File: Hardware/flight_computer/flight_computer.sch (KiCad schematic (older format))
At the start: 15 parts

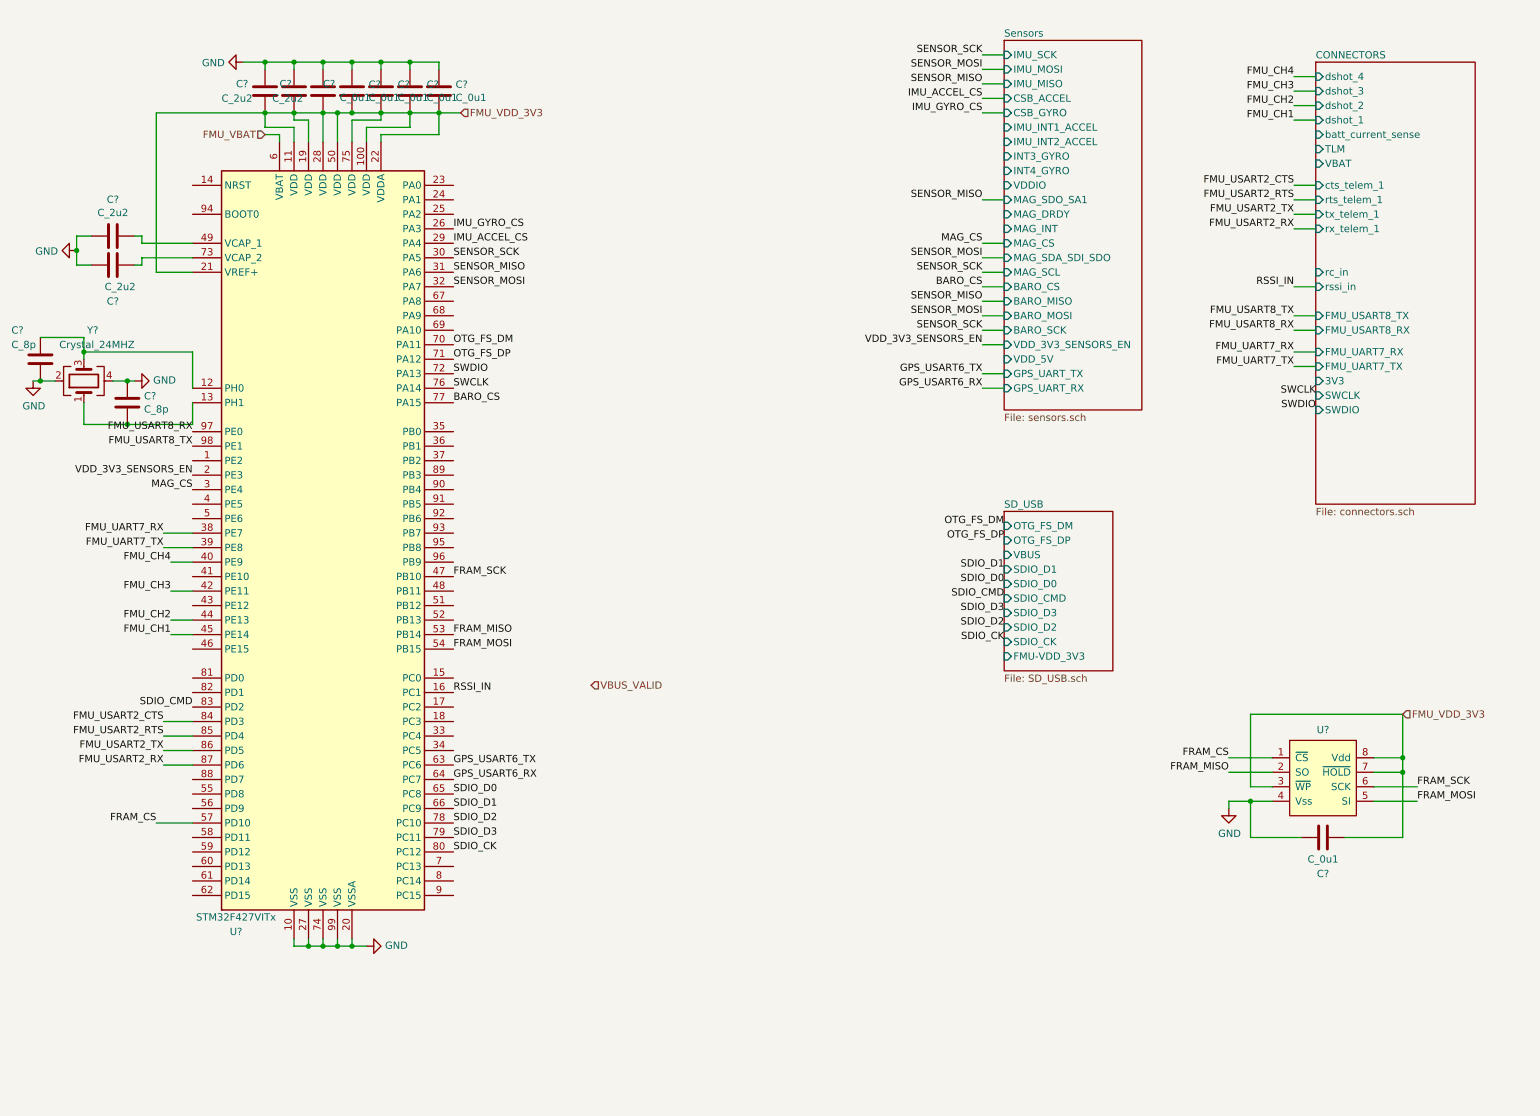
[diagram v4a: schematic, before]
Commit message: Updates drdy pins and rc connections
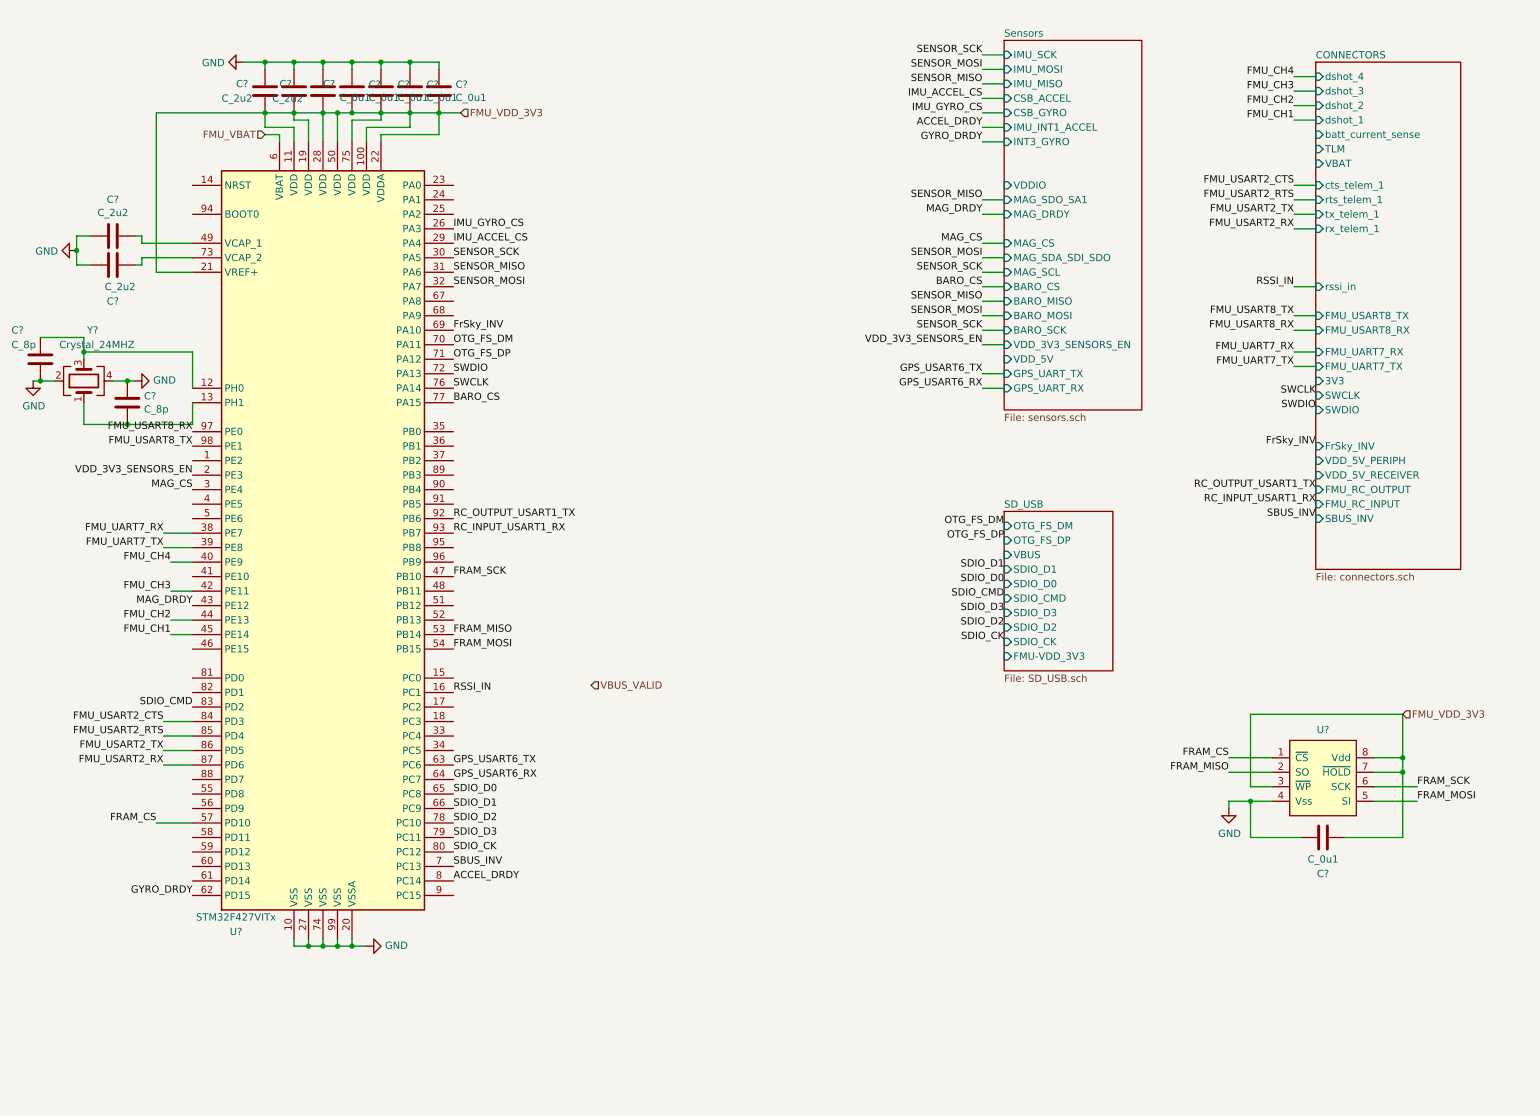
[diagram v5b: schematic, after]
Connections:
- net MAG_DRDY: now reaches U?.43 (PE12)
- net GYRO_DRDY: now reaches U?.62 (PD15)
- net FrSky_INV: now reaches U?.69 (PA10)
- net SBUS_INV: now reaches U?.7 (PC13)
- net ACCEL_DRDY: now reaches U?.8 (PC14)
- net RC_OUTPUT_USART1_TX: now reaches U?.92 (PB6)
- net RC_INPUT_USART1_RX: now reaches U?.93 (PB7)
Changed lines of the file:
@@
 F6 "CSB_GYRO" I L 7550 1150 50
 F7 "IMU_INT1_ACCEL" I L 7550 1250 50
-F8 "IMU_INT2_ACCEL" I L 7550 1350 50
-F9 "INT3_GYRO" I L 7550 1450 50
-F10 "INT4_GYRO" I L 7550 1550 50
+F9 "INT3_GYRO" I L 7550 1350 50
 F11 "VDDIO" I L 7550 1650 50
 F12 "MAG_SDO_SA1" I L 7550 1750 50
 F13 "MAG_DRDY" I L 7550 1850 50
-F14 "MAG_INT" I L 7550 1950 50
 F15 "MAG_CS" I L 7550 2050 50
 F16 "MAG_SDA_SDI_SDO" I L 7550 2150 50
@@
 VDD_3V3_SENSORS_EN
 $Sheet
-S 9700 800  1100 3050
+S 9700 800  1000 3500
 U 5F7684E9
 F0 "CONNECTORS" 50
@@
 F11 "cts_telem_1" I L 9700 1650 50
 F12 "rts_telem_1" I L 9700 1750 50
-F13 "rc_in" I L 9700 2250 50
 F14 "rssi_in" I L 9700 2350 50
 F15 "FMU_UART7_RX" I L 9700 2800 50
@@
 F20 "FMU_USART8_TX" I L 9700 2550 50
 F21 "FMU_USART8_RX" I L 9700 2650 50
+F22 "FrSky_INV" I L 9700 3450 50
+F23 "VDD_5V_PERIPH" I L 9700 3550 50
+F24 "VDD_5V_RECEIVER" I L 9700 3650 50
+F25 "FMU_RC_OUTPUT" I L 9700 3750 50
+F26 "FMU_RC_INPUT" I L 9700 3850 50
+F27 "SBUS_INV" I L 9700 3950 50
 $EndSheet
 Text Label 7400 1050 2    50   ~ 0
@@
 Text Label 9700 3100 2    50   ~ 0
 SWCLK
+Text Label 3750 6450 0    50   ~ 0
+ACCEL_DRDY
+Text Label 1950 6550 2    50   ~ 0
+GYRO_DRDY
+Text Label 1950 4550 2    50   ~ 0
+MAG_DRDY
+Text Label 7400 1250 2    50   ~ 0
+ACCEL_DRDY
+Text Label 7400 1350 2    50   ~ 0
+GYRO_DRDY
+Text Label 7400 1850 2    50   ~ 0
+MAG_DRDY
+Wire Wire Line
+	7550 1850 7400 1850
+Wire Wire Line
+	7550 1250 7400 1250
+Wire Wire Line
+	7550 1350 7400 1350
+Text Label 3750 6350 0    50   ~ 0
+SBUS_INV
+Text Label 9700 3950 2    50   ~ 0
+SBUS_INV
+Text Label 3750 2650 0    50   ~ 0
+FrSky_INV
+Text Label 9700 3450 2    50   ~ 0
+FrSky_INV
+Text Label 3750 4050 0    50   ~ 0
+RC_INPUT_USART1_RX
+Text Label 3750 3950 0    50   ~ 0
+RC_OUTPUT_USART1_TX
+Text Label 9700 3850 2    50   ~ 0
+RC_INPUT_USART1_RX
+Text Label 9700 3750 2    50   ~ 0
+RC_OUTPUT_USART1_TX
 $EndSCHEMATC

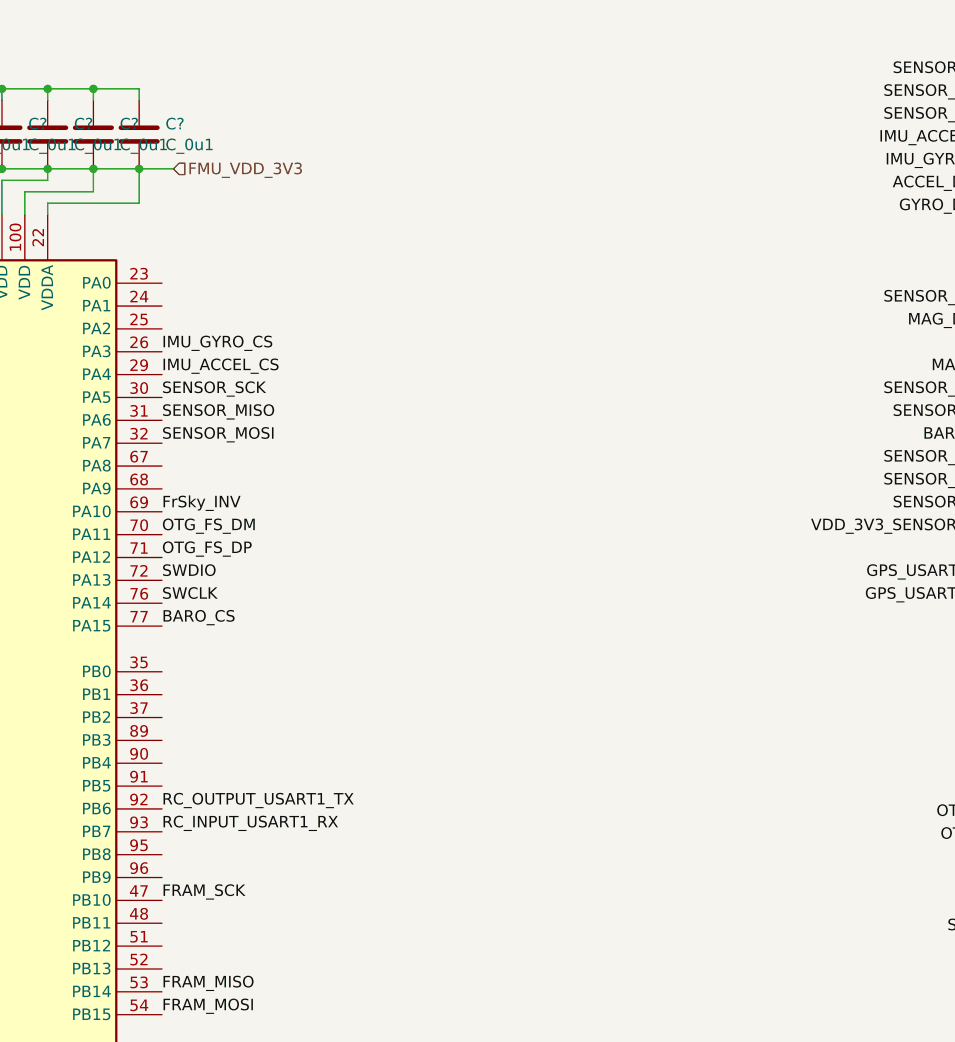
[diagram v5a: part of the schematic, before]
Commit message: Adds raspi i2c
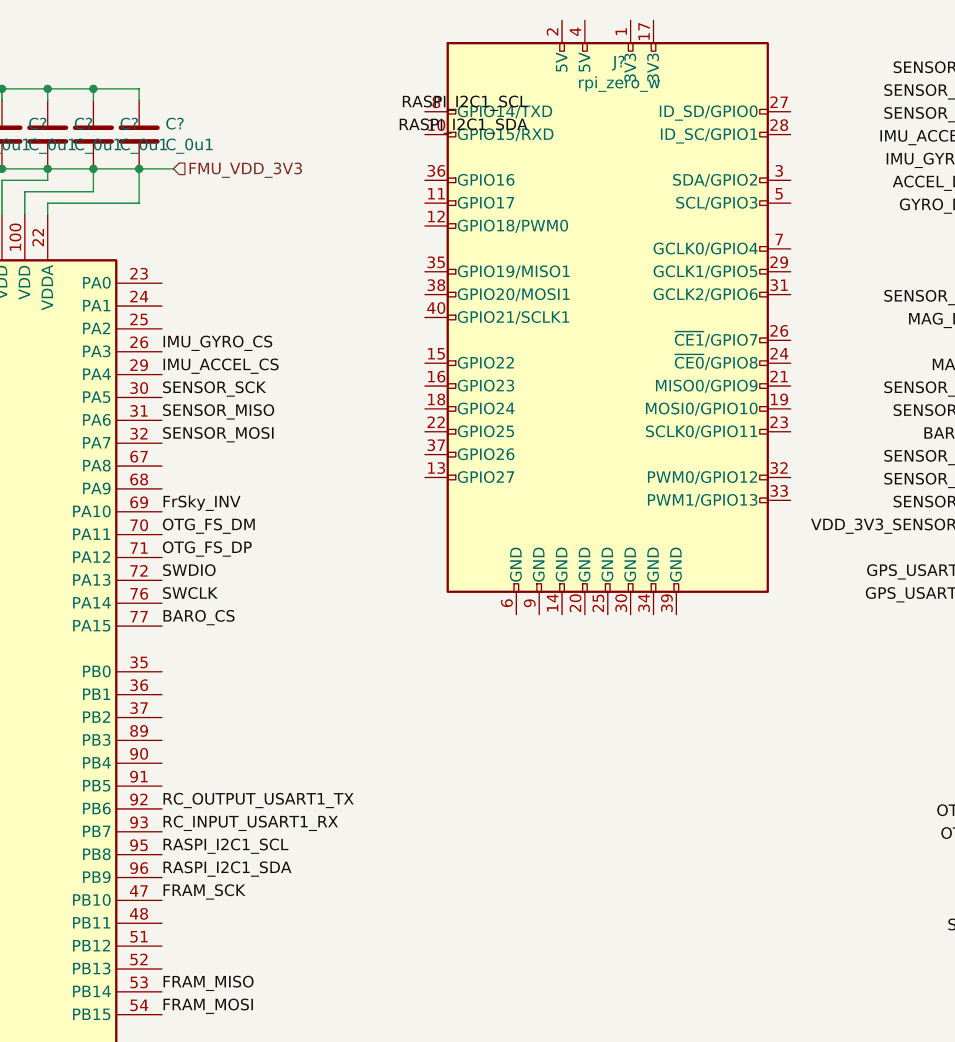
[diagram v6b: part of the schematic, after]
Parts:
- added J?: rpi_zero_w, drone_footprints:rpi_zero_w, symbol openDrone_parts:rpi_zero_w
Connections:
- net RASPI_I2C1_SCL: now reaches U?.95 (PB8)
- net RASPI_I2C1_SDA: now reaches U?.96 (PB9)
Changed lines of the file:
@@
 Text Label 9700 3750 2    50   ~ 0
 RC_OUTPUT_USART1_TX
+Text Label 3750 4150 0    50   ~ 0
+RASPI_I2C1_SCL
+Text Label 3750 4250 0    50   ~ 0
+RASPI_I2C1_SDA
+Text Label 5350 900  2    50   ~ 0
+RASPI_I2C1_SCL
+Text Label 5350 1000 2    50   ~ 0
+RASPI_I2C1_SDA
+$Comp
+L openDrone_parts:rpi_zero_w J?
+U 1 1 5F812ED0
+P 5700 1800
+F 0 "J?" H 5750 2917 50  0000 C CNN
+F 1 "rpi_zero_w" H 5750 2826 50  0000 C CNN
+F 2 "drone_footprints:rpi_zero_w" H 5700 1800 50  0001 C CNN
+F 3 "~" H 5700 1800 50  0001 C CNN
+	1    5700 1800
+	1    0    0    -1
+$EndComp
 $EndSCHEMATC

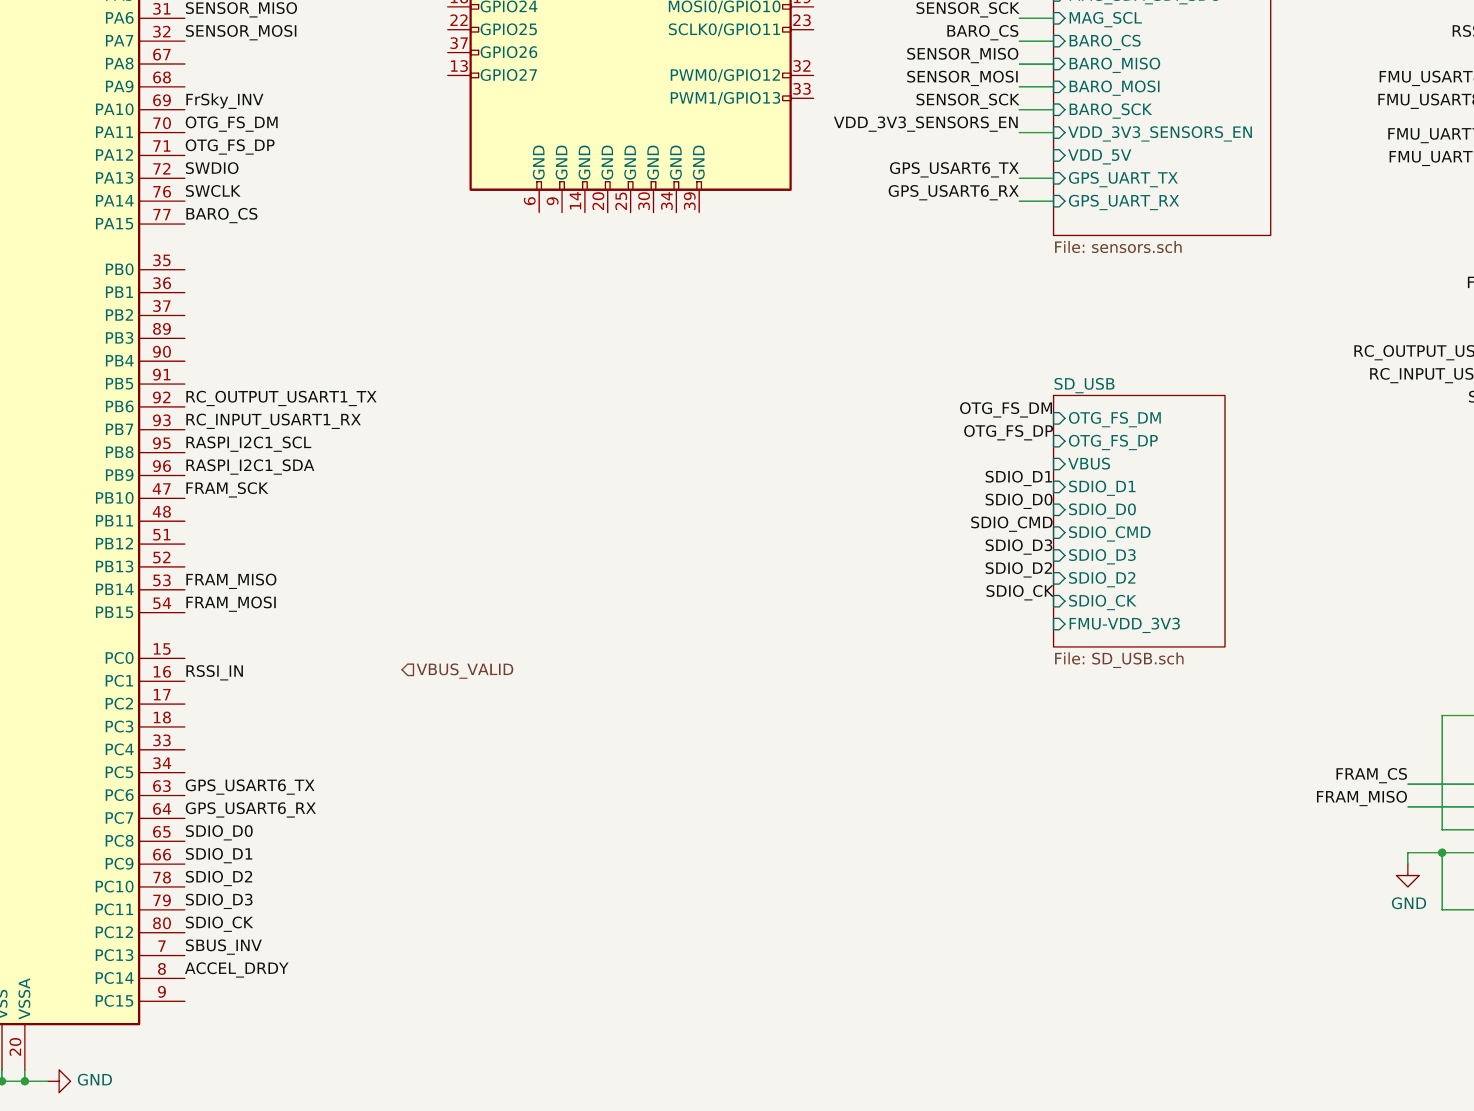
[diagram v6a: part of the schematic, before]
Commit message: Adds buck converters
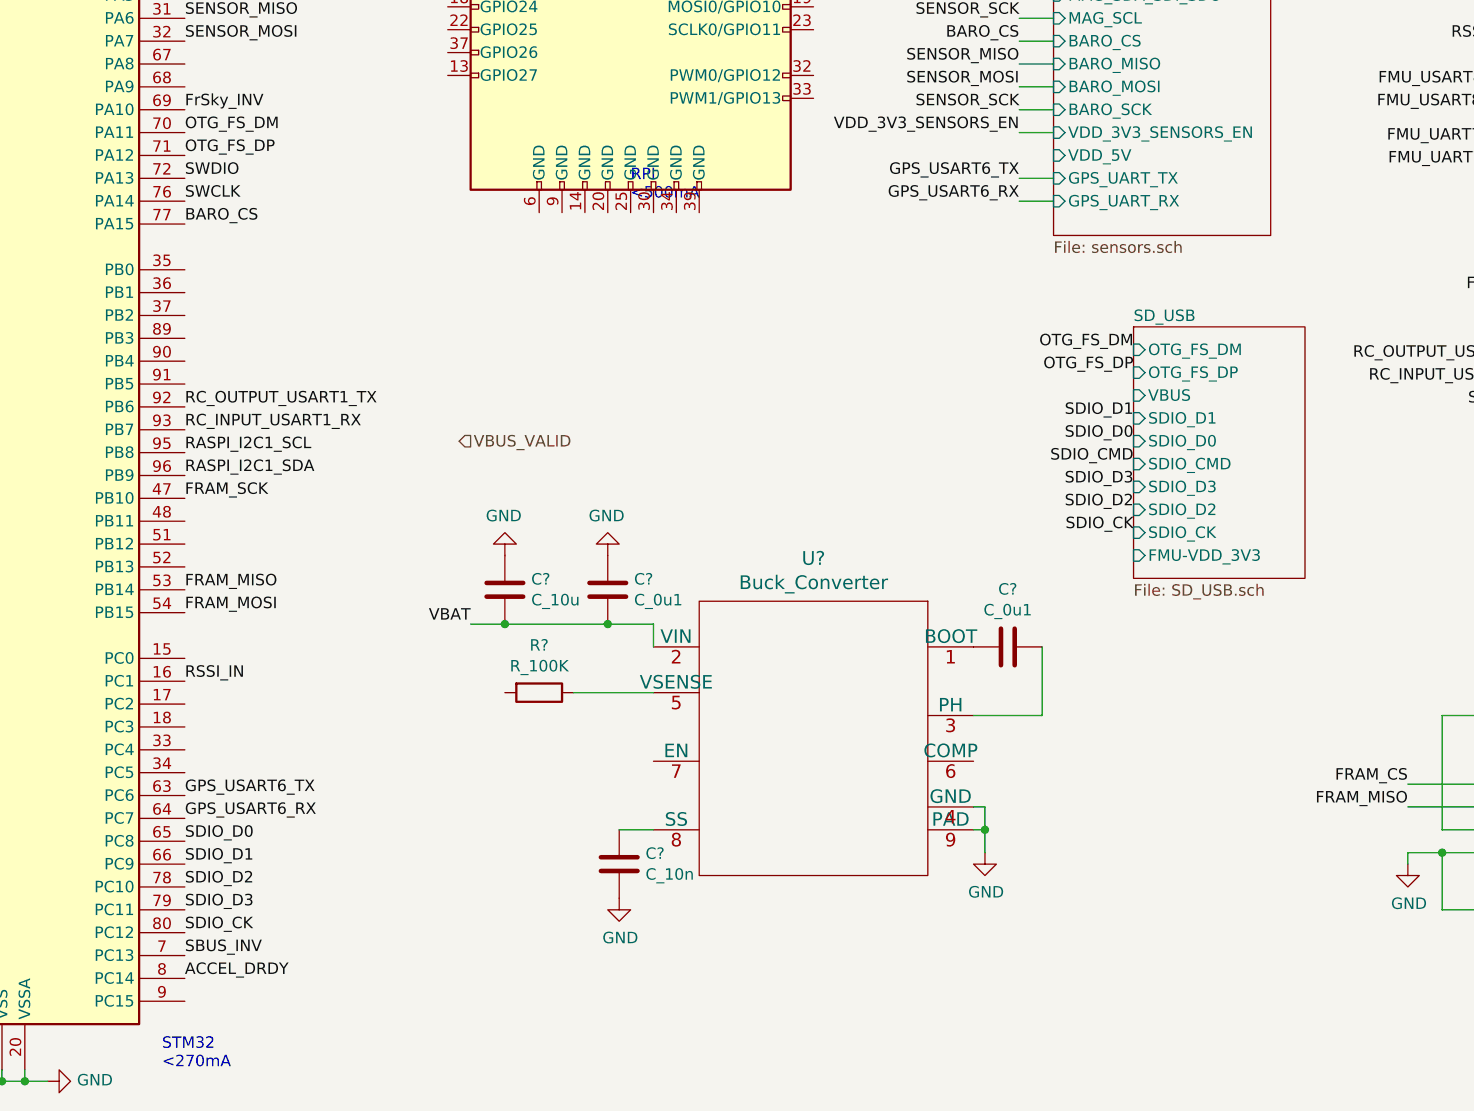
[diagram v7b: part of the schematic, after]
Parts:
- added C? (x2): C_0u1, Capacitors_SMD:C_0805, symbol openDrone_parts:C_0u1
- added C?: C_10n, Capacitors_SMD:C_0805, symbol openDrone_parts:C_10n
- added C?: C_10u, Capacitors_SMD:C_0805, symbol openDrone_parts:C_10u
- added R?: R_100K, Resistors_SMD:R_0805, symbol openDrone_parts:R_100K
- added U?: Buck_Converter, drone_footprints:TPS54336ADDAR, symbol openDrone_parts:Buck_Converter
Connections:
- net GND: now also C?.1, C?.1, C?.2, U?.4 (GND), U?.9 (PAD)
- new net: C?.2, U?.1 (BOOT)
- new net: C?.1, U?.3 (PH)
- new net: R?.1, U?.5 (VSENSE)
- new net: C?.1, U?.8 (SS)
- new net VBAT: C?.2, C?.2, U?.2 (VIN)
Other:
- note added: "RPI\n<500mA"
- note added: "STM32\n<270mA"
